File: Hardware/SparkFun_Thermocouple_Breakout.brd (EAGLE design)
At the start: 30 x 19.8 mm, 15 parts, among them U1 MAX31855K

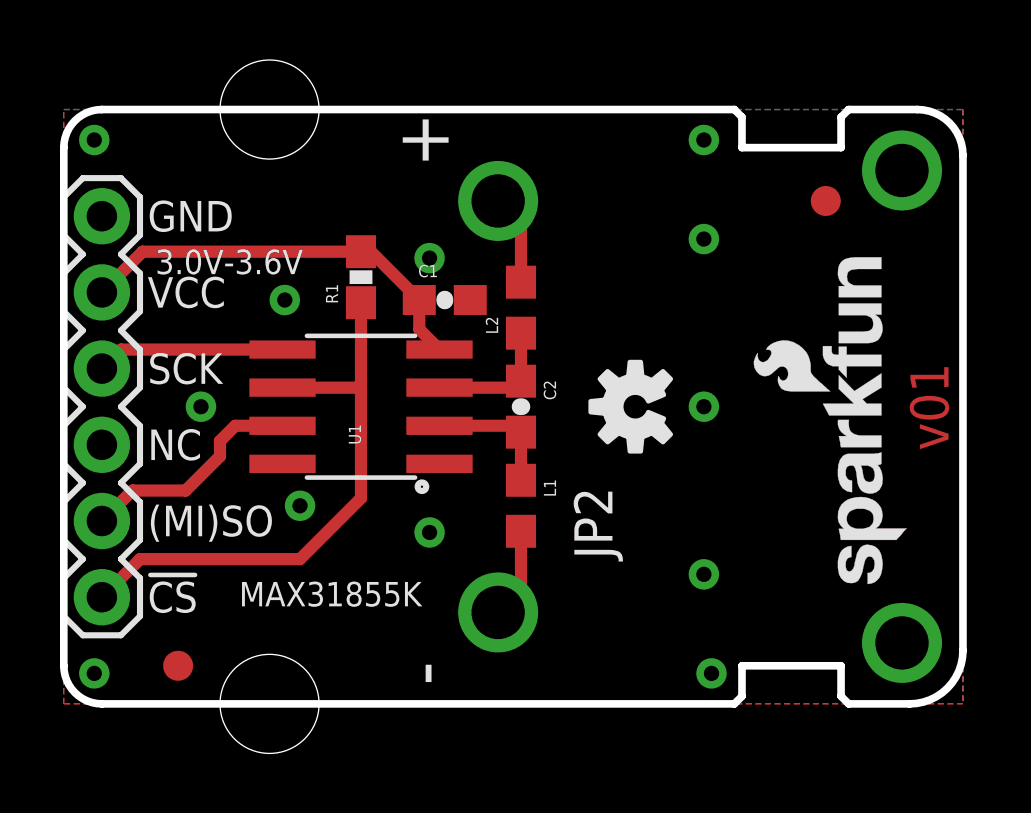
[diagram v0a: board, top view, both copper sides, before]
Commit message: Removed acid trap and nudged a via
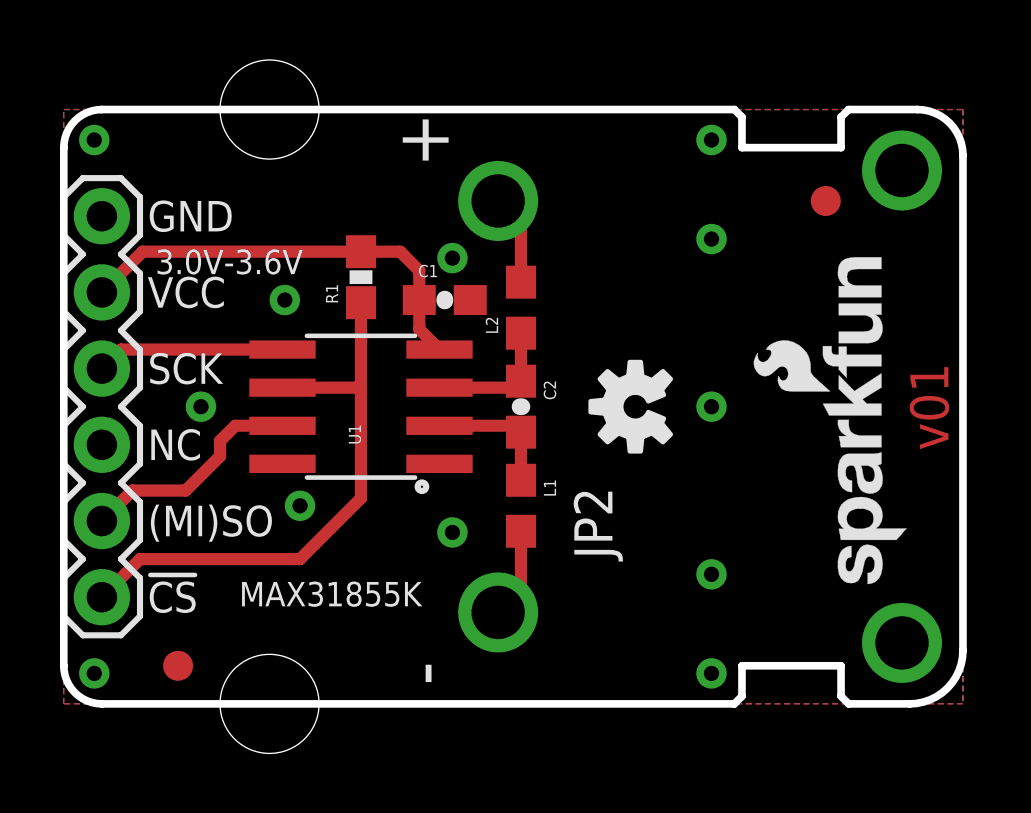
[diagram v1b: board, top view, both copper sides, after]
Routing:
- net VCC: track 14.0 -> 14.5 mm
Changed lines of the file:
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@@
 <layer number="20" name="Dimension" color="15" fill="1" visible="yes" active="yes"/>
 <layer number="21" name="tPlace" color="16" fill="1" visible="yes" active="yes"/>
-<layer number="22" name="bPlace" color="14" fill="1" visible="yes" active="yes"/>
+<layer number="22" name="bPlace" color="14" fill="1" visible="no" active="yes"/>
 <layer number="23" name="tOrigins" color="15" fill="1" visible="yes" active="yes"/>
 <layer number="24" name="bOrigins" color="15" fill="1" visible="yes" active="yes"/>
@@
 <contactref element="JP1" pad="1"/>
 <via x="7.366" y="13.462" extent="1-16" drill="0.508"/>
-<via x="21.336" y="18.796" extent="1-16" drill="0.508"/>
+<via x="21.59" y="18.796" extent="1-16" drill="0.508"/>
 <via x="1.016" y="18.796" extent="1-16" drill="0.508"/>
 <via x="1.016" y="1.016" extent="1-16" drill="0.508"/>
 <via x="21.59" y="1.016" extent="1-16" drill="0.508"/>
-<via x="21.336" y="15.494" extent="1-16" drill="0.508"/>
-<via x="21.336" y="9.906" extent="1-16" drill="0.508"/>
-<via x="21.336" y="4.318" extent="1-16" drill="0.508"/>
-<via x="12.192" y="5.715" extent="1-16" drill="0.508"/>
-<via x="12.192" y="14.859" extent="1-16" drill="0.508"/>
+<via x="21.59" y="15.494" extent="1-16" drill="0.508"/>
+<via x="21.59" y="9.906" extent="1-16" drill="0.508"/>
+<via x="21.59" y="4.318" extent="1-16" drill="0.508"/>
+<via x="12.954" y="5.715" extent="1-16" drill="0.508"/>
+<via x="12.954" y="14.859" extent="1-16" drill="0.508"/>
 </signal>
 <signal name="N$7">
@@
 <wire x1="9.906" y1="15.074" x2="2.628" y2="15.074" width="0.4064" layer="1"/>
 <wire x1="2.628" y1="15.074" x2="1.27" y2="13.716" width="0.4064" layer="1"/>
-<wire x1="9.906" y1="15.074" x2="10.238" y2="15.074" width="0.4064" layer="1"/>
-<wire x1="10.238" y1="15.074" x2="11.85" y2="13.462" width="0.4064" layer="1"/>
+<wire x1="9.906" y1="15.074" x2="11.215" y2="15.074" width="0.4064" layer="1"/>
+<wire x1="11.215" y1="15.074" x2="11.85" y2="14.439" width="0.4064" layer="1"/>
+<wire x1="11.85" y1="14.439" x2="11.85" y2="13.462" width="0.4064" layer="1"/>
 </signal>
 <signal name="N$3">

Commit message: Added a second logo to the back, mirrored the revision, & added the version number to the frame that disappeared with the new version of the frame
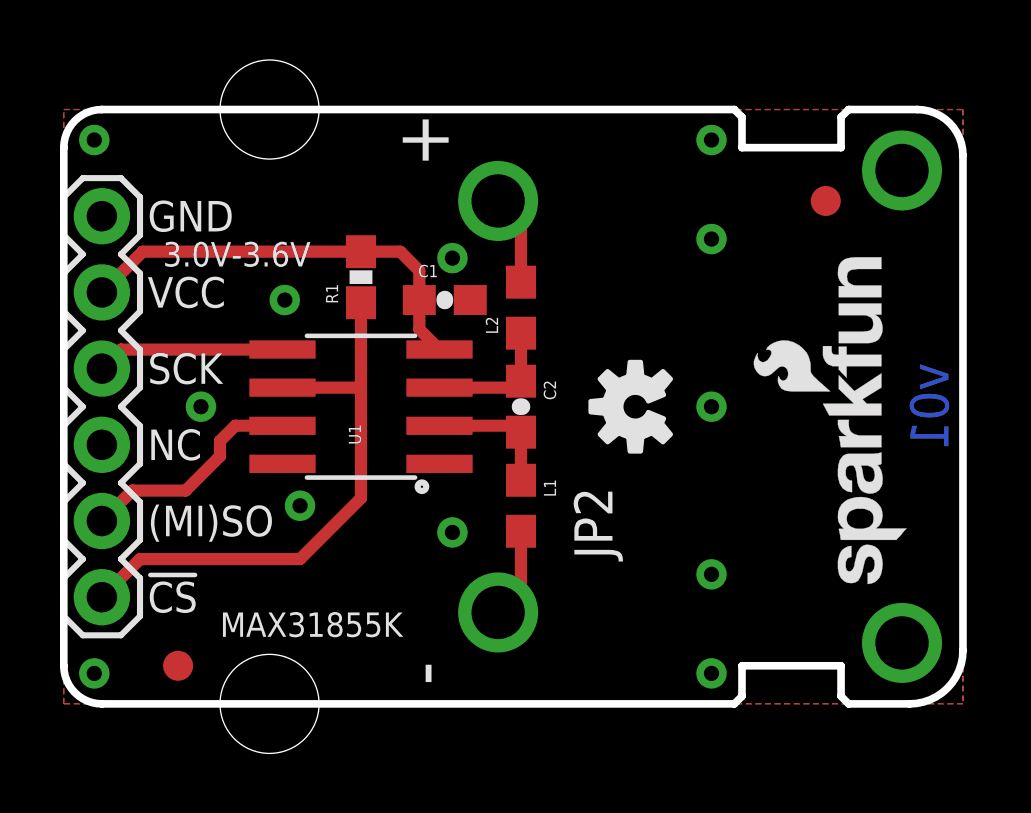
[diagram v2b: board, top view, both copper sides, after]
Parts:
- added LOGO3: SFE_LOGO_NAME_FLAME.1_INCH, SparkFun-Aesthetics:SFE_LOGO_NAME_FLAME_.1
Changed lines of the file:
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@@
 <layer number="20" name="Dimension" color="15" fill="1" visible="yes" active="yes"/>
 <layer number="21" name="tPlace" color="16" fill="1" visible="yes" active="yes"/>
-<layer number="22" name="bPlace" color="14" fill="1" visible="no" active="yes"/>
+<layer number="22" name="bPlace" color="14" fill="1" visible="yes" active="yes"/>
 <layer number="23" name="tOrigins" color="15" fill="1" visible="yes" active="yes"/>
 <layer number="24" name="bOrigins" color="15" fill="1" visible="yes" active="yes"/>
@@
 <layer number="45" name="Holes" color="7" fill="1" visible="yes" active="yes"/>
 <layer number="46" name="Milling" color="3" fill="1" visible="no" active="yes"/>
-<layer number="47" name="Measures" color="7" fill="1" visible="yes" active="yes"/>
+<layer number="47" name="Measures" color="7" fill="1" visible="no" active="yes"/>
 <layer number="48" name="Document" color="7" fill="1" visible="no" active="yes"/>
-<layer number="49" name="Reference" color="7" fill="1" visible="no" active="yes"/>
+<layer number="49" name="Reference" color="7" fill="1" visible="yes" active="yes"/>
 <layer number="50" name="dxf" color="7" fill="1" visible="no" active="no"/>
 <layer number="51" name="tDocu" color="6" fill="1" visible="yes" active="yes"/>
@@
 <text x="2.794" y="16.256" size="1.016" layer="22" font="vector" ratio="15" rot="MR0" align="center-right">GND</text>
 <text x="2.794" y="13.716" size="1.016" layer="22" font="vector" ratio="15" rot="MR0" align="center-right">VCC</text>
-<text x="5.842" y="4.064" size="0.8128" layer="21" font="vector" ratio="15" rot="R180" align="bottom-right">MAX31855K</text>
+<text x="5.207" y="3.048" size="0.8128" layer="21" font="vector" ratio="15" rot="R180" align="bottom-right">MAX31855K</text>
 <text x="9.906" y="22.225" size="1.27" layer="47" ratio="15">All units in inches</text>
-<text x="3.048" y="14.732" size="0.8128" layer="21" font="vector" ratio="15" align="center-left">3.0V-3.6V</text>
-<polygon width="0.4064" layer="41">
+<text x="3.302" y="14.986" size="0.8128" layer="21" font="vector" ratio="15" align="center-left">3.0V-3.6V</text>
+<polygon width="0.4064" layer="42">
 <vertex x="29.972" y="11.43"/>
 <vertex x="28.448" y="11.43"/>
@@
 <elements>
 <element name="FRAME1" library="SparkFun-Aesthetics" package="CREATIVE_COMMONS" value="&gt;VERSION" x="-8.5598" y="-12.6746" smashed="yes">
-<attribute name="VERSION" value="v01" x="29.4894" y="9.906" size="1.27" layer="1" font="vector" ratio="15" rot="SR90" align="bottom-center"/>
-<attribute name="DESIGNER" value="Brent Wilkins" x="21.4122" y="-12.6746" size="1.778" layer="51"/>
+<attribute name="VERSION" value="v01" x="29.4894" y="9.906" size="1.27" layer="16" font="vector" ratio="15" rot="SMR270" align="bottom-center"/>
+<attribute name="DESIGNER" value="Brent Wilkins" x="21.4122" y="-12.6746" size="1.778" layer="51" font="vector"/>
 </element>
 <element name="STANDOFF4" library="SparkFun-Electromechanical" package="STAND-OFF" value="STAND-OFF" x="6.858" y="19.812"/>
@@
 </element>
 <element name="JP2" library="Testing" package="PCC-SMP" value="PCB_THERMOCOUPLE" x="14.478" y="9.906" rot="R90"/>
+<element name="LOGO3" library="SparkFun-Aesthetics" package="SFE_LOGO_NAME_FLAME_.1" value="SFE_LOGO_NAME_FLAME.1_INCH" x="28.194" y="15.367" rot="MR270"/>
 </elements>
 <signals>

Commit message: Added more logos!
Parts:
- added LOGO4: OSHW-LOGOS, SparkFun-Aesthetics:OSHW-LOGO-S
